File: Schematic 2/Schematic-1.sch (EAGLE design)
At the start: 37 parts, among them IC1 7805T, IC3 MCP23017SO, Q1 BSS138, Q2 BSS138, U2 LMV358, U3 LMV324

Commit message: Final tweaks to plugable Tiva board
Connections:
- new net N$9: IC3.GPA1, JP4.2
- net N$3: no longer IC3.GPA1
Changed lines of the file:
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@@
 </variantdefs>
 <classes>
-<class number="0" name="default" width="0" drill="0">
+<class number="0" name="default" width="0.00508125" drill="0">
 <clearance class="0" value="0.2"/>
 </class>
@@
 <label x="127" y="12.7" size="1.016" layer="95" rot="R180" xref="yes"/>
 <pinref part="C1" gate="G$1" pin="1"/>
+<junction x="132.08" y="12.7"/>
 </segment>
 </net>
@@
 <pinref part="JP1" gate="A" pin="2"/>
 <wire x1="139.7" y1="-15.24" x2="137.16" y2="-15.24" width="0.1524" layer="91"/>
+<junction x="139.7" y="-12.7"/>
+<junction x="137.16" y="-15.24"/>
 </segment>
 <segment>
@@
 <pinref part="R4" gate="G$1" pin="1"/>
 <wire x1="185.42" y1="66.04" x2="195.58" y2="66.04" width="0.1524" layer="91"/>
+<label x="190.5" y="66.04" size="1.778" layer="95" rot="R270" xref="yes"/>
 </segment>
 <segment>
@@
 <label x="162.56" y="12.7" size="1.016" layer="95" xref="yes"/>
 <pinref part="C2" gate="G$1" pin="1"/>
+<junction x="157.48" y="12.7"/>
 </segment>
 <segment>
@@
 <wire x1="149.86" y1="-12.7" x2="152.4" y2="-12.7" width="0.1524" layer="91"/>
 <pinref part="JP2" gate="A" pin="2"/>
+<junction x="152.4" y="-15.24"/>
+<junction x="152.4" y="-12.7"/>
 </segment>
 </net>
@@
 <pinref part="JP4" gate="G$1" pin="1"/>
 <wire x1="254" y1="48.26" x2="264.16" y2="48.26" width="0.1524" layer="91"/>
-<pinref part="IC3" gate="G$1" pin="GPA1"/>
-<wire x1="254" y1="45.72" x2="264.16" y2="45.72" width="0.1524" layer="91"/>
-<wire x1="264.16" y1="45.72" x2="264.16" y2="48.26" width="0.1524" layer="91"/>
 </segment>
 </net>
@@
 </segment>
 </net>
+<net name="N$9" class="0">
+<segment>
+<pinref part="IC3" gate="G$1" pin="GPA1"/>
+<pinref part="JP4" gate="G$1" pin="2"/>
+<wire x1="254" y1="45.72" x2="264.16" y2="45.72" width="0.1524" layer="91"/>
+</segment>
+</net>

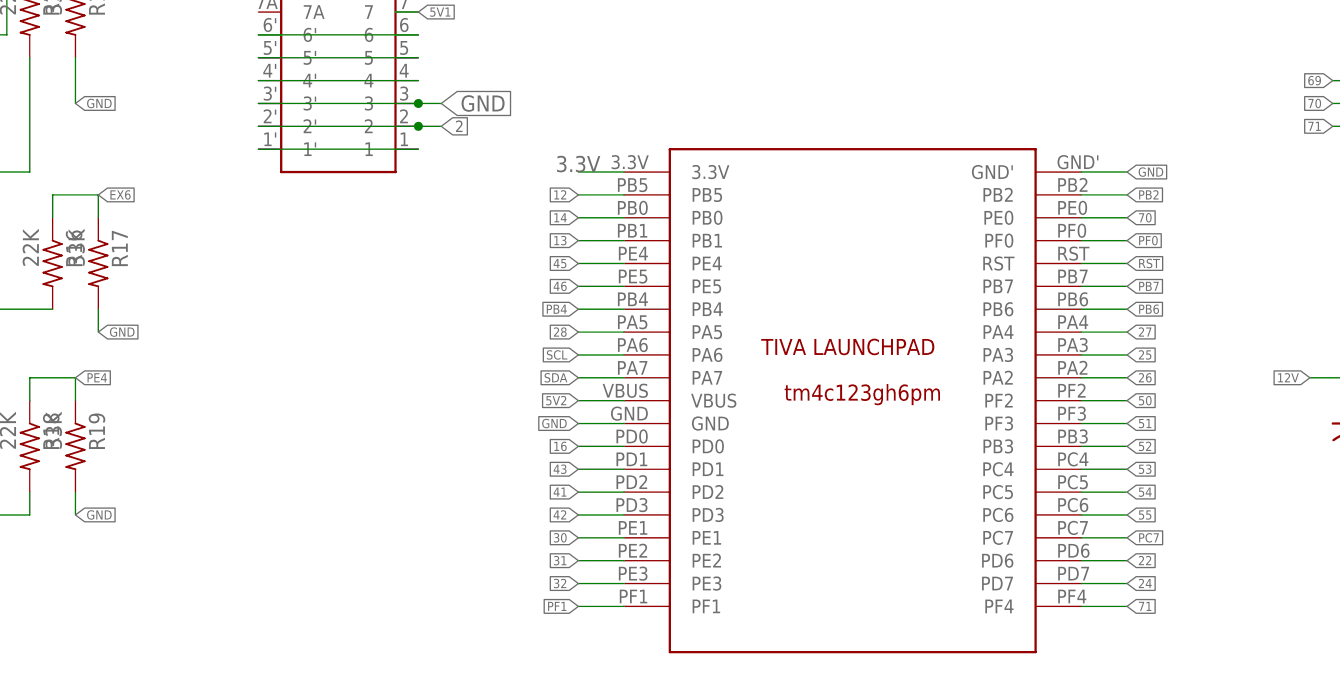
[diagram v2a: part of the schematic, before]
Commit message: Plugable TIVA changes on 13-06-17
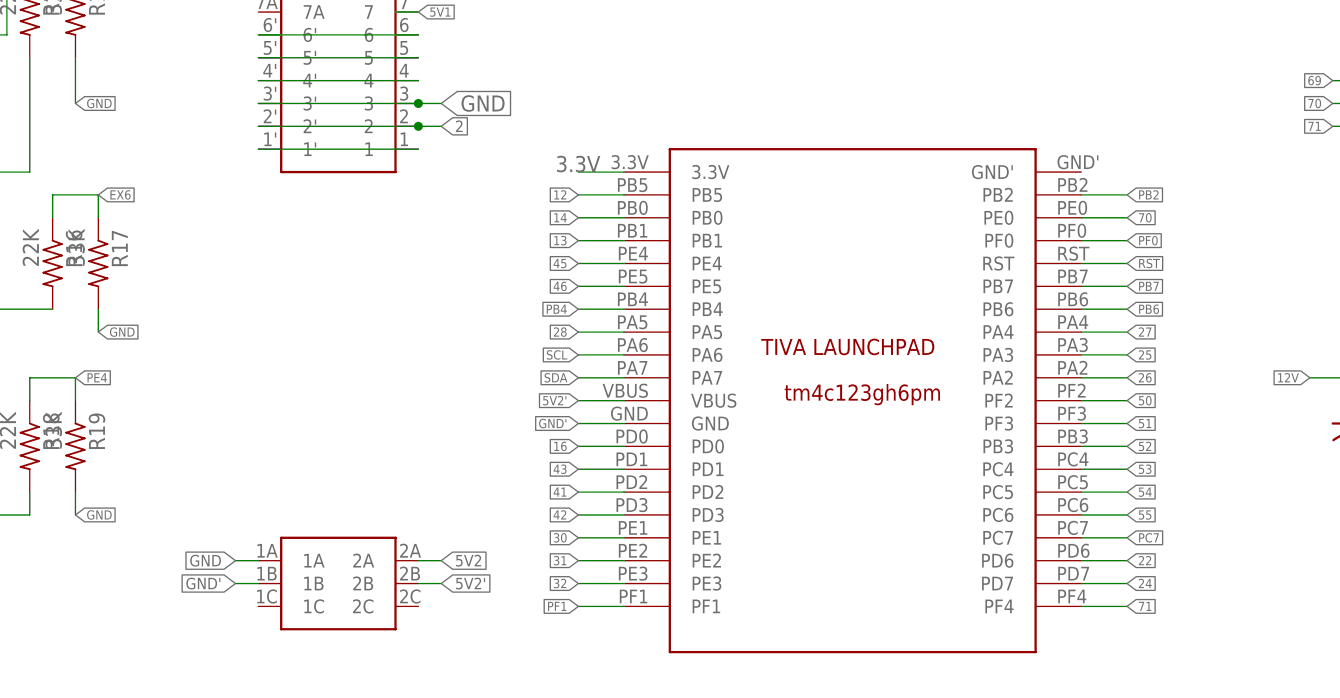
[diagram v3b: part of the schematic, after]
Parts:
- added U$3: SELF-LOCKING_SWITCHSELF-LOCKING_SWITCH, Switch_Self-locking:SELF-LOCKING_SWITCHSELF-LOCKING_SWITCH
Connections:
- new net 5V2': U$2.VBUS, U$3.2B
- new net GND': U$2.GND, U$3.1B
- net 5V2: now also U$3.2A; no longer U$2.VBUS
- net GND: now also U$3.1A; no longer U$2.GND, U$2.GND'
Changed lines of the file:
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@@
 <part name="JP6" library="adafruit" deviceset="PINHD-1X1" device=""/>
 <part name="JP7" library="adafruit" deviceset="PINHD-1X1" device=""/>
+<part name="U$3" library="Switch_Self-locking" deviceset="SELF-LOCKING_SWITCH" device="SELF-LOCKING_SWITCH"/>
 </parts>
 <sheets>
@@
 <instance part="JP6" gate="G$1" x="172.72" y="45.72"/>
 <instance part="JP7" gate="G$1" x="172.72" y="40.64"/>
+<instance part="U$3" gate="G$1" x="60.96" y="-22.86"/>
 </instances>
 <busses>
@@
 </net>
 <net name="GND" class="1">
-<segment>
-<pinref part="U$2" gate="G$1" pin="GND"/>
-<wire x1="50.8" y1="7.62" x2="45.72" y2="7.62" width="0.1524" layer="91"/>
-<label x="45.72" y="7.62" size="1.016" layer="95" rot="R180" xref="yes"/>
-</segment>
-<segment>
-<pinref part="U$2" gate="G$1" pin="GND'"/>
-<wire x1="101.6" y1="35.56" x2="106.68" y2="35.56" width="0.1524" layer="91"/>
-<label x="106.68" y="35.56" size="1.016" layer="95" xref="yes"/>
-</segment>
 <segment>
 <pinref part="U$4" gate="G$1" pin="GND"/>
@@
 <junction x="27.94" y="43.18"/>
 <label x="30.48" y="43.18" size="1.778" layer="95" xref="yes"/>
+</segment>
+<segment>
+<wire x1="10.16" y1="-7.62" x2="7.62" y2="-7.62" width="0.1524" layer="91"/>
+<label x="7.62" y="-7.62" size="1.27" layer="95" rot="R180" xref="yes"/>
+<pinref part="U$3" gate="G$1" pin="1A"/>
 </segment>
 </net>
@@
 </segment>
 <segment>
+<wire x1="27.94" y1="-7.62" x2="30.48" y2="-7.62" width="0.1524" layer="91"/>
+<label x="30.48" y="-7.62" size="1.27" layer="95" xref="yes"/>
+<pinref part="U$3" gate="G$1" pin="2A"/>
+</segment>
+</net>
+<net name="N$9" class="0">
+<segment>
+<pinref part="IC3" gate="G$1" pin="GPA1"/>
+<pinref part="JP4" gate="G$1" pin="2"/>
+<wire x1="254" y1="45.72" x2="264.16" y2="45.72" width="0.1524" layer="91"/>
+</segment>
+</net>
+<net name="GND'" class="1">
+<segment>
+<pinref part="U$2" gate="G$1" pin="GND"/>
+<wire x1="50.8" y1="7.62" x2="45.72" y2="7.62" width="0.1524" layer="91"/>
+<label x="45.72" y="7.62" size="1.016" layer="95" rot="R180" xref="yes"/>
+</segment>
+<segment>
+<wire x1="10.16" y1="-10.16" x2="7.62" y2="-10.16" width="0.1524" layer="91"/>
+<label x="7.62" y="-10.16" size="1.27" layer="95" rot="R180" xref="yes"/>
+<pinref part="U$3" gate="G$1" pin="1B"/>
+</segment>
+</net>
+<net name="5V2'" class="1">
+<segment>
 <pinref part="U$2" gate="G$1" pin="VBUS"/>
 <wire x1="50.8" y1="10.16" x2="45.72" y2="10.16" width="0.1524" layer="91"/>
 <label x="45.72" y="10.16" size="1.016" layer="95" rot="R180" xref="yes"/>
 </segment>
-</net>
-<net name="N$9" class="0">
-<segment>
-<pinref part="IC3" gate="G$1" pin="GPA1"/>
-<pinref part="JP4" gate="G$1" pin="2"/>
-<wire x1="254" y1="45.72" x2="264.16" y2="45.72" width="0.1524" layer="91"/>
-</segment>
-</net>
+<segment>
+<wire x1="27.94" y1="-10.16" x2="30.48" y2="-10.16" width="0.1524" layer="91"/>
+<label x="30.48" y="-10.16" size="1.27" layer="95" xref="yes"/>
+<pinref part="U$3" gate="G$1" pin="2B"/>
+</segment>
+</net>

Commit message: Version 2 of Plug and Play Board
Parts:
- added LED1, LED10, LED11, LED12, LED13, LED14, LED15, LED16, LED2, LED3, LED4, LED5, LED6, LED7, LED8, LED9: (no value), adafruit:LEDSMT1206
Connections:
- net 5V2: now also U$3.2C; no longer U$3.2A
- net GND: now also LED1.C, LED10.C, LED11.C, LED12.C, LED13.C, LED14.C, LED15.C, LED16.C, LED2.C, LED3.C, LED4.C, LED5.C, LED6.C, LED7.C, LED8.C, LED9.C
- net N$10: now also LED5.A
- net N$11: now also LED6.A
- net N$12: now also LED7.A
- net N$15: now also LED8.A
- net N$20: now also LED9.A
- net N$21: now also LED10.A
- net N$22: now also LED11.A
- net N$23: now also LED12.A
- net N$24: now also LED13.A
- net N$25: now also LED15.A
- net N$28: now also LED14.A
- net N$29: now also LED16.A
- net N$3: now also LED1.A
- net N$7: now also LED3.A
- net N$8: now also LED4.A
- net N$9: now also LED2.A
